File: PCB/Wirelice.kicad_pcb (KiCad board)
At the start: 2 copper layers, 337.7 x 122.7 mm, 176 parts, among them J1 SWD, J2 USB_C_Receptacle_USB2.0, J3 Unified DB, J5 Battery, SW1 Rotary_Encoder_Switch, SW29 SW_Push, U1 nRF52840_holyiot_18010, U2 SRV05-4, U3 TP4056, U4 FS8205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

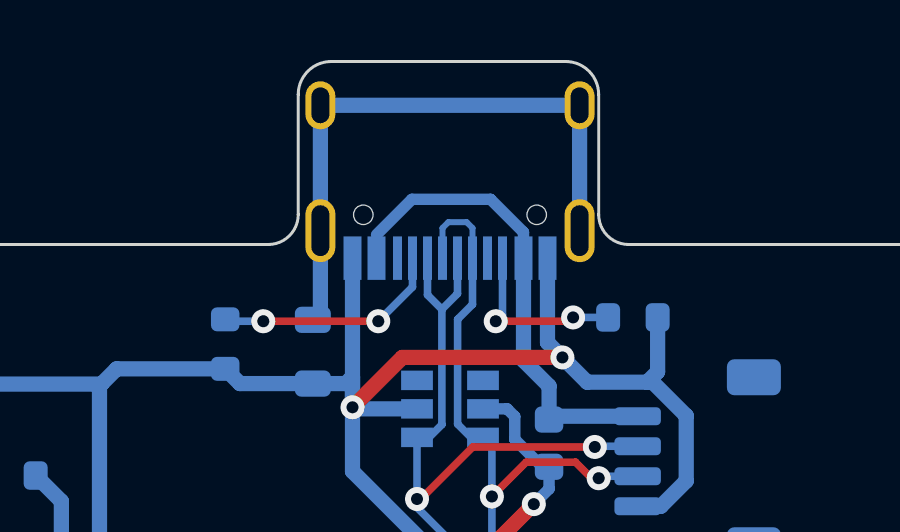
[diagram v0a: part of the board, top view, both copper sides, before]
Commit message: Add Plate and Back
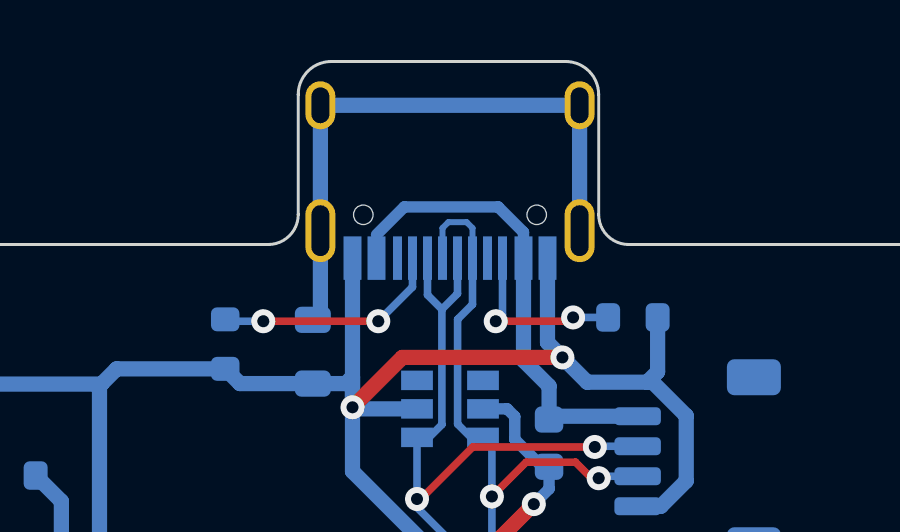
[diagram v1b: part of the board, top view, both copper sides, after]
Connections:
- U1 pad 36: EXTRA4 -> unconnected-(U1-Pad36)
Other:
- board text added: "GND"
- board text added: "SWCLK"
- board text added: "SWDIO"
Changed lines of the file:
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@@
   (net 108 "/STDBY")
   (net 109 "/CHRG")
-  (net 110 "EXTRA4")
+  (net 110 "unconnected-(U1-Pad36)")
   (net 111 "unconnected-(U2-Pad4)")
   (net 112 "unconnected-(U2-Pad3)")
@@
     (property "Sheetfile" "Wirelice.kicad_sch")
     (property "Sheetname" "")
-    (attr through_hole)
+    (property "exclude_from_bom" "")
+    (attr through_hole exclude_from_bom)
     (fp_text reference "H1" (at 0 0) (layer "B.SilkS") hide
       (effects (font (size 1.27 1.27) (thickness 0.15)) (justify mirror))
@@
     (tags "capacitor")
     (property "LCSC" "C14663")
-    (property "Package" "")
     (property "Sheetfile" "Wirelice.kicad_sch")
     (property "Sheetname" "")
-    (property "Specification" "")
     (attr smd)
     (fp_text reference "C1" (at 2.286 0 180) (layer "B.SilkS")
@@
     (tags "capacitor")
     (property "LCSC" "C15849")
-    (property "Package" "")
     (property "Sheetfile" "Wirelice.kicad_sch")
     (property "Sheetname" "")
-    (property "Specification" "")
     (attr smd)
     (fp_text reference "C23" (at -3.061 0.013) (layer "B.SilkS")
@@
       (net 97 "COL8") (pinfunction "P0.09") (pintype "bidirectional"))
     (pad "36" smd rect locked (at 6.75 4.6 180) (size 1.524 0.7) (layers "B.Cu" "B.Paste" "B.Mask")
-      (net 110 "EXTRA4") (pinfunction "P0.10") (pintype "bidirectional"))
+      (net 110 "unconnected-(U1-Pad36)") (pinfunction "P0.10") (pintype "bidirectional+no_connect"))
     (pad "37" smd rect locked (at 6.75 5.7 180) (size 1.524 0.7) (layers "B.Cu" "B.Paste" "B.Mask")
       (net 1 "GND") (pinfunction "GND") (pintype "power_in"))
@@
     (descr "LED SMD 0805 (2012 Metric), square (rectangular) end terminal, IPC_7351 nominal, (Body size source: https://docs.google.com/spreadsheets/d/1BsfQQcO9C6DZCsRaXUlFlo91Tg2WpOkGARC1WS5S8t0/edit?usp=sharing), generated with kicad-footprint-generator")
     (tags "LED")
+    (property "LCSC" "C2297")
     (property "Sheetfile" "Wirelice.kicad_sch")
     (property "Sheetname" "")
@@
     (tags "capacitor")
     (property "LCSC" "C14663")
-    (property "Package" "")
     (property "Sheetfile" "Wirelice.kicad_sch")
     (property "Sheetname" "")
-    (property "Specification" "")
     (attr smd)
     (fp_text reference "C12" (at 3.048 -0.889 180) (layer "B.SilkS")
@@
     (descr "LED SMD 0805 (2012 Metric), square (rectangular) end terminal, IPC_7351 nominal, (Body size source: https://docs.google.com/spreadsheets/d/1BsfQQcO9C6DZCsRaXUlFlo91Tg2WpOkGARC1WS5S8t0/edit?usp=sharing), generated with kicad-footprint-generator")
     (tags "LED")
+    (property "LCSC" "C84256")
     (property "Sheetfile" "Wirelice.kicad_sch")
     (property "Sheetname" "")
@@
     (tags "capacitor")
     (property "LCSC" "C14663")
-    (property "Package" "")
     (property "Sheetfile" "Wirelice.kicad_sch")
     (property "Sheetname" "")
-    (property "Specification" "")
     (attr smd)
     (fp_text reference "C24" (at -3.061 0.013) (layer "B.SilkS")
@@
     (property "Sheetfile" "Wirelice.kicad_sch")
     (property "Sheetname" "")
-    (attr smd)
+    (property "exclude_from_bom" "")
+    (attr smd exclude_from_bom)
     (fp_text reference "J5" (at 0 5.8 90) (layer "B.SilkS")
       (effects (font (size 1 1) (thickness 0.15)) (justify mirror))
@@
     (property "Sheetfile" "Wirelice.kicad_sch")
     (property "Sheetname" "")
-    (property "Specification" "")
     (attr smd)
     (fp_text reference "C18" (at -3.95 0.013) (layer "B.SilkS")
@@
     (tags "resistor")
     (property "LCSC" "C22775")
-    (property "Package" "")
     (property "Sheetfile" "Wirelice.kicad_sch")
     (property "Sheetname" "")
@@
     (property "Sheetfile" "Wirelice.kicad_sch")
     (property "Sheetname" "")
-    (attr exclude_from_pos_files)
+    (property "exclude_from_bom" "")
+    (attr exclude_from_pos_files exclude_from_bom)
     (fp_text reference "SW29" (at 0 -4.4958 45) (layer "Dwgs.User")
       (effects (font (size 1 1) (thickness 0.15)))
@@
     (tags "capacitor")
     (property "LCSC" "C15849")
-    (property "Package" "")
     (property "Sheetfile" "Wirelice.kicad_sch")
     (property "Sheetname" "")
-    (property "Specification" "")
     (attr smd)
     (fp_text reference "C22" (at -2.807 0.013) (layer "B.SilkS")
@@
     (tags "capacitor")
     (property "LCSC" "C19666 ")
-    (property "Package" "")
     (property "Sheetfile" "Wirelice.kicad_sch")
     (property "Sheetname" "")
-    (property "Specification" "")
     (attr smd)
     (fp_text reference "C20" (at 0 2.286 180) (layer "B.SilkS")
@@
     (fp_line (start 0.8 -0.4) (end -0.8 -0.4) (layer "B.Fab") (width 0.1))
     (pad "1" smd roundrect locked (at -0.7875 0 270) (size 0.875 0.95) (layers "B.Cu" "B.Paste" "B.Mask") (roundrect_rratio 0.25)
-      (net 87 "VBUS"))
+      (net 87 "VBUS") (pintype "passive"))
     (pad "2" smd roundrect locked (at 0.7875 0 270) (size 0.875 0.95) (layers "B.Cu" "B.Paste" "B.Mask") (roundrect_rratio 0.25)
-      (net 2 "+5V"))
+      (net 2 "+5V") (pintype "passive"))
     (model "${KISYS3DMOD}/Fuse.3dshapes/Fuse_0603_1608Metric.wrl"
       (offset (xyz 0 0 0))
@@
     (property "Sheetfile" "Wirelice.kicad_sch")
     (property "Sheetname" "")
-    (attr through_hole)
+    (property "exclude_from_bom" "")
+    (attr through_hole exclude_from_bom)
     (fp_text reference "J1" (at 0 2.33) (layer "B.SilkS")
       (effects (font (size 1 1) (thickness 0.15)) (justify mirror))
@@
     (tags "capacitor")
     (property "LCSC" "C19666 ")
-    (property "Package" "")
     (property "Sheetfile" "Wirelice.kicad_sch")
     (property "Sheetname" "")
-    (property "Specification" "")
     (attr smd)
     (fp_text reference "C21" (at -2.807 0.013) (layer "B.SilkS")
@@
     (tags "resistor")
     (property "LCSC" "C21190")
-    (property "Package" "")
     (property "Sheetfile" "Wirelice.kicad_sch")
     (property "Sheetname" "")
@@
     (effects (font (size 2 2) (thickness 0.45)) (justify mirror))
   )
+  (gr_text "SWDIO" (at 216.281 148.336) (layer "B.SilkS")
+    (effects (font (size 1 1) (thickness 0.2)) (justify mirror))
+  )
   (gr_text "JLCJLCJLCJLC" (at 210.82 84.455) (layer "B.SilkS")
     (effects (font (size 0.75 0.75) (thickness 0.15)) (justify mirror))
   )
+  (gr_text "GND" (at 216.37625 143.1925) (layer "B.SilkS")
+    (effects (font (size 1 1) (thickness 0.2)) (justify mirror))
+  )
   (gr_text "+" (at 184.15 101.6) (layer "B.SilkS")
     (effects (font (size 2 2) (thickness 0.45)) (justify mirror))
@@
     (effects (font (size 2 2) (thickness 0.3)) (justify left mirror))
   )
+  (gr_text "SWCLK" (at 216.154 145.669) (layer "B.SilkS")
+    (effects (font (size 1 1) (thickness 0.2)) (justify mirror))
+  )
   (gr_text "CHARGING\n        ▼" (at 214.3125 102.362) (layer "B.SilkS")
     (effects (font (size 0.75 0.75) (thickness 0.15)) (justify left mirror))
@@
   (segment (start 212.57 89.563) (end 212.57 87.686) (width 0.254) (layer "B.Cu") (net 86))
   (segment (start 214.23125 92.95625) (end 214.122 93.0655) (width 0.508) (layer "B.Cu") (net 87))
+  (segment (start 208.37 86.905) (end 209.296 85.979) (width 0.381) (layer "B.Cu") (net 87))
   (segment (start 214.122 91.948) (end 214.122 93.0655) (width 0.508) (layer "B.Cu") (net 87))
-  (segment (start 209.55 85.725) (end 212.173124 85.725) (width 0.381) (layer "B.Cu") (net 87))
-  (segment (start 217.075 92.95625) (end 214.23125 92.95625) (width 0.508) (layer "B.Cu") (net 87))
-  (segment (start 208.37 86.905) (end 209.55 85.725) (width 0.381) (layer "B.Cu") (net 87))
   (segment (start 213.27 86.821876) (end 213.27 87.686) (width 0.381) (layer "B.Cu") (net 87))
+  (segment (start 217.075 92.95625) (end 214.23125 92.95625) (width 0.508) (layer "B.Cu") (net 87))
+  (segment (start 209.296 85.979) (end 212.427124 85.979) (width 0.381) (layer "B.Cu") (net 87))
   (segment (start 213.27 87.686) (end 213.27 91.096) (width 0.508) (layer "B.Cu") (net 87))
   (segment (start 213.27 91.096) (end 214.122 91.948) (width 0.508) (layer "B.Cu") (net 87))
-  (segment (start 212.173124 85.725) (end 213.27 86.821876) (width 0.381) (layer "B.Cu") (net 87))
+  (segment (start 212.427124 85.979) (end 213.27 86.821876) (width 0.381) (layer "B.Cu") (net 87))
   (segment (start 191.925 101.457) (end 190.881 100.413) (width 0.508) (layer "B.Cu") (net 88))
   (segment (start 192.278 96.647) (end 192.278 94.882) (width 0.508) (layer "B.Cu") (net 88))

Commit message: Updated stuff
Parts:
- moved D43 5.16 mm to (191.8, 149.5)
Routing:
- net ROW2: track 392.1 -> 389.1 mm
- net Net-(D43-Pad2): track 8.35 -> 5.80 mm
